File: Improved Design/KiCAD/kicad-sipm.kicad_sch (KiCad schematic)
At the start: 26 parts, among them J1 Conn_01x05, J2 Conn_Coaxial, U1 OPA847IDBVT, U2 OPA842IDBVT

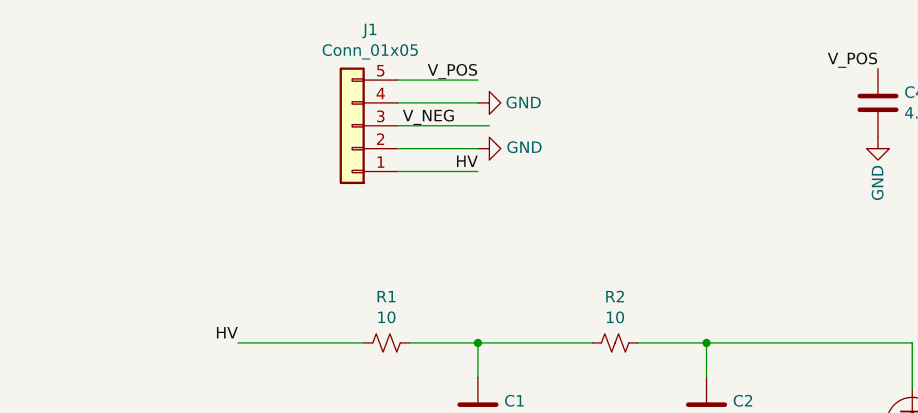
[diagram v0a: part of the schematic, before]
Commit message: Add part number for the pin header and the matching plug
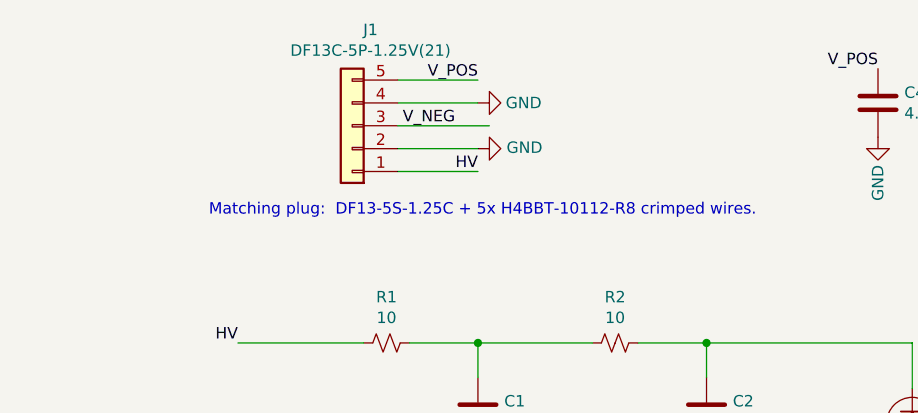
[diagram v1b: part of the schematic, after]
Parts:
- J1: value Conn_01x05 -> DF13C-5P-1.25V(21); Digikey Part (none) -> H126001CT-ND
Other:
- note added: "Matching plug: DF13-5S-1.25C + 5x H4BBT-10112-R8 crimped wires."
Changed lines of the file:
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@@
+    (effects (font (size 1.27 1.27)) (justify right bottom))
+  )
+  (text "Matching plug:  DF13-5S-1.25C + 5x H4BBT-10112-R8 crimped wires."
+    (at 86.8172 46.99 0)
     (effects (font (size 1.27 1.27)) (justify right bottom))
   )
@@
     (in_bom yes) (on_board yes)
     (property "Reference" "J1" (id 0) (at 43.942 26.1682 0))
-    (property "Value" "Conn_01x05" (id 1) (at 43.942 28.4669 0))
+    (property "Value" "DF13C-5P-1.25V(21)" (id 1) (at 43.942 28.4669 0))
     (property "Footprint" "footprints:DF13C-5P-1.25V21" (id 2) (at 41.91 36.83 0)
       (effects (font (size 1.27 1.27)) hide)
@@
       (effects (font (size 1.27 1.27)) hide)
     )
+    (property "Digikey Part" "H126001CT-ND" (id 4) (at 41.91 36.83 0)
+      (effects (font (size 1.27 1.27)) hide)
+    )

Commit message: Correct PZC values
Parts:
- L1: value 0.4u -> 0.47u
- R5: value 100 -> 220
- R6: value 10 -> 28
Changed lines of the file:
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@@
       (effects (font (size 1.27 1.27)) (justify left))
     )
-    (property "Value" "0.4u" (id 1) (at 182.753 105.289 0)
+    (property "Value" "0.47u" (id 1) (at 182.753 105.289 0)
       (effects (font (size 1.27 1.27)) (justify left))
     )
@@
     (in_bom yes) (on_board yes)
     (property "Reference" "R5" (id 0) (at 173.99 91.4592 90))
-    (property "Value" "100" (id 1) (at 173.99 89.161 90))
+    (property "Value" "220" (id 1) (at 173.99 89.161 90))
     (property "Footprint" "footprints:R_0402_1005Metric" (id 2) (at 173.99 86.36 0)
       (effects (font (size 1.27 1.27)) hide)
@@
     (in_bom yes) (on_board yes)
     (property "Reference" "R6" (id 0) (at 186.7092 95.25 90))
-    (property "Value" "10" (id 1) (at 184.411 95.25 90))
+    (property "Value" "28" (id 1) (at 184.411 95.25 90))
     (property "Footprint" "footprints:R_0402_1005Metric" (id 2) (at 181.61 95.25 0)
       (effects (font (size 1.27 1.27)) hide)
